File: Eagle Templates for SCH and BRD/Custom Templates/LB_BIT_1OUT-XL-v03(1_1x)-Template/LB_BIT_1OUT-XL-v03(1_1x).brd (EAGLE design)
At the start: 21.4 x 42.4 mm, 9 parts, among them U6 LV321SOT23-5

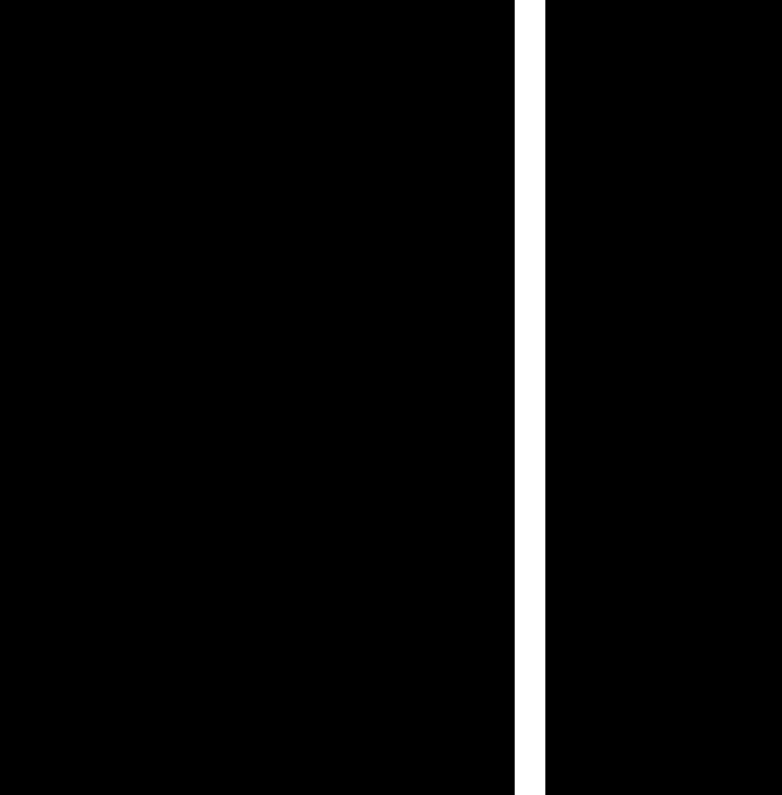
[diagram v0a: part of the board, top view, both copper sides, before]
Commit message: added bitlab logo and made minor changes to board templates. Updated littlebits library.
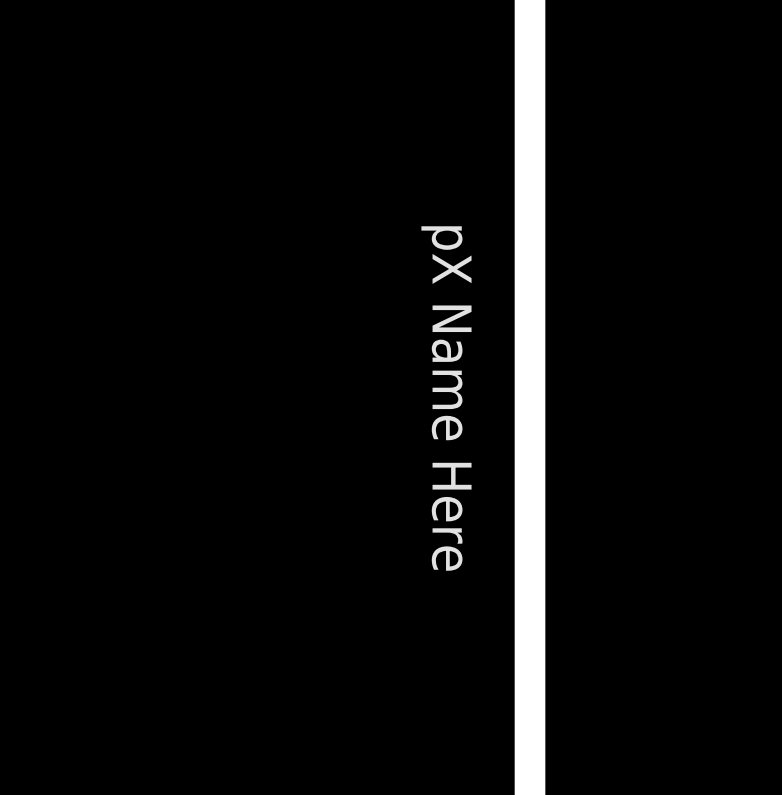
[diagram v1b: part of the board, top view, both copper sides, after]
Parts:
- added U$2: (no value), LITTLEBITS:BITLAB-LOGO
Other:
- board text added: "pX Name Here"
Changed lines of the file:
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@@
 <dimension x1="3.025" y1="4.635" x2="23.425" y2="4.635" x3="13.225" y3="-14.915" textsize="1.778" layer="47" dtype="horizontal"/>
 <text x="22.2" y="4.9" size="0.8128" layer="16" font="vector" ratio="12" rot="MR90">revX</text>
+<text x="21.3" y="23.1" size="1.3" layer="21" font="vector" rot="SR270" align="center">pX Name Here</text>
 </plain>
 <attributes>
@@
 <element name="U$4" library="LITTLEBITS" package="LB_PWR_LEGS" value="" x="3.225" y="34.84"/>
 <element name="FRAME1" library="LITTLEBITS" package="FABDWG01-OHW" value="FRAME-LETTER" x="0" y="0"/>
+<element name="U$2" library="LITTLEBITS" package="BITLAB-LOGO" value="" x="19.9" y="27" rot="R270"/>
 </elements>
 <signals>

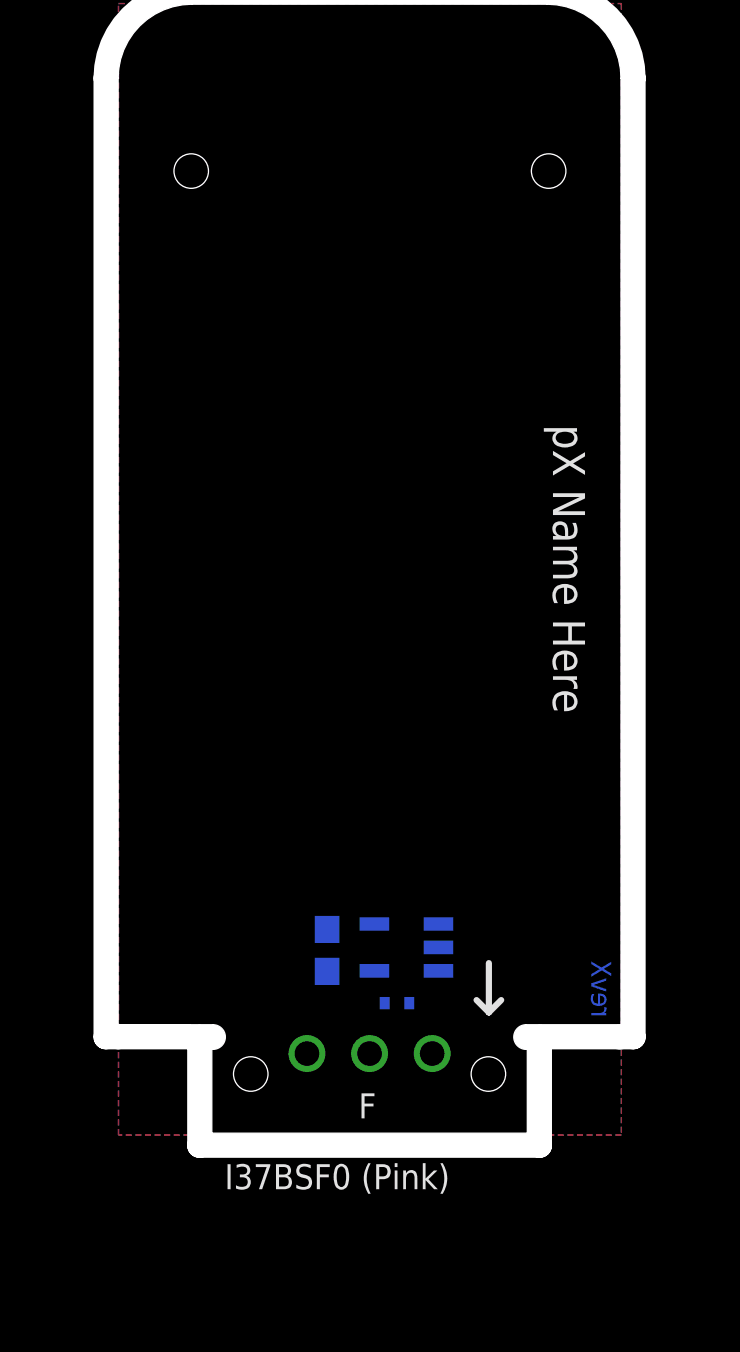
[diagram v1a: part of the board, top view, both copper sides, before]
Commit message: Updated templates
- Added ferrite beads
- Moved text and annotations off of Nets layer
- Minor layout changes
- Removed I/O/W prefix from reference designators
- Removed output stage components from output bits
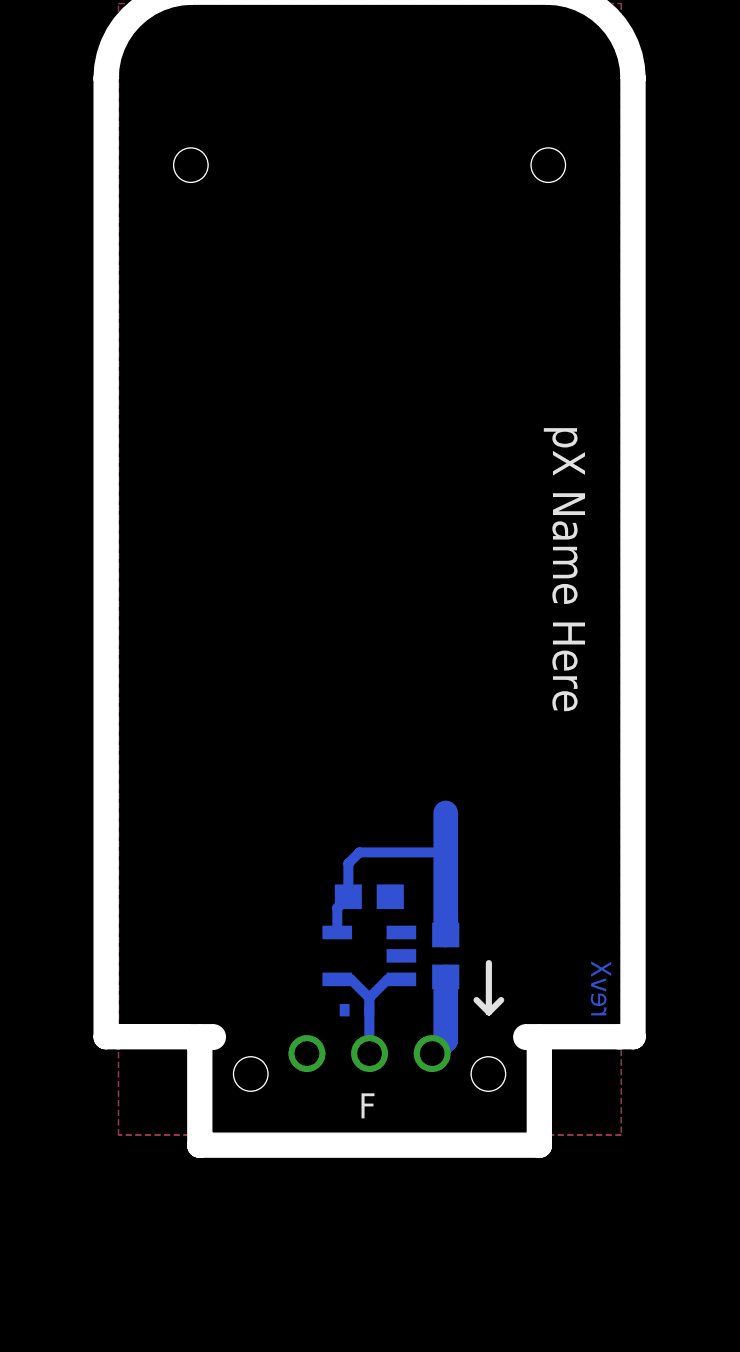
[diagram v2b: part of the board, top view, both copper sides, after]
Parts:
- removed I?C4: 1.0uF, LITTLEBITS:CAP-0603
- removed I?TVS6: ESD9B5.0ST5G, LITTLEBITS:SOD-923
- removed U6: LV321SOT23-5, LITTLEBITS:SOT23-5
- added C1: 1.0uF, LITTLEBITS:CAP-0603
- added FB1: FERRITE-BEAD0603, LITTLEBITS:R0603
- added TVS1: ESD9B5.0ST5G, LITTLEBITS:SOD-923
- added U1: LV321SOT23-5, LITTLEBITS:SOT23-5
- FRAME1: value FRAME-LETTER -> FRAME-LETTERWHITEMASK; device LITTLEBITS:FABDWG01-OHW -> LITTLEBITS:FABDWG01-WHITEMASK
- moved U$4 5.86 mm to (6.61, 39.6)
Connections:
- new net N$1: FB1.1, I37BSF1.VCC
- net GND: now also C1.1, I37BSF1.GND, TVS1.1, U1.2; no longer I?C4.1, I?TVS6.1, U6.2
- net N$12: now also U1.1; no longer U6.1
- net SIG_OUT: now also I37BSF1.SIG, TVS1.2, U1.3, U1.4; no longer I?TVS6.2, U6.3, U6.4
- net VCC: now also C1.2, FB1.2, U1.5; no longer I?C4.2, U6.5
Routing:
- net VCC: track 0.00 -> 12.1 mm
- net SIG_OUT: track 0.00 -> 5.49 mm
- net N$1: track 0.00 -> 3.34 mm
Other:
- board text removed: "I37BSF0 (Pink)"
